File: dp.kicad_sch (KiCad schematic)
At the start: 27 parts, among them J1 DisplayPort_Mini_47272-0001, U1 74AVC4T245_UQFN, U2 FIN1019MTC, U3 TPD4E05U06QDQARQ1_ALT, U4 824012823

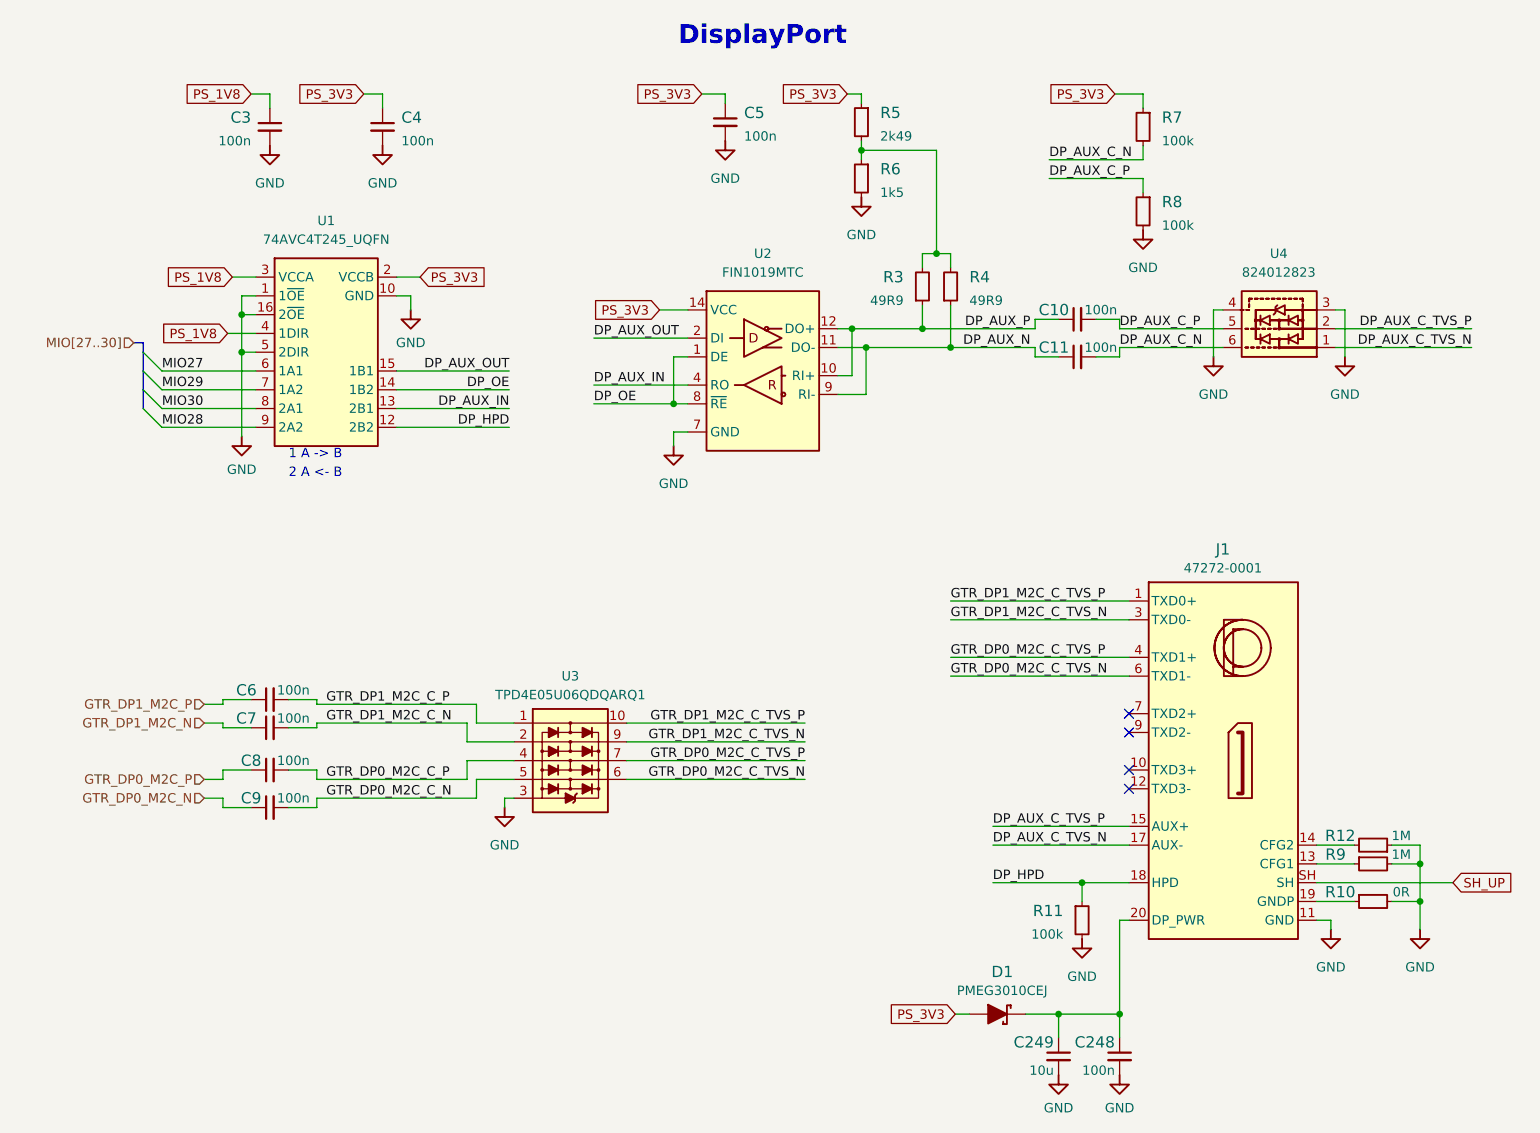
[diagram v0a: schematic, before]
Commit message: [#47975] Add missing ESD diode pass for USB 3.0 and DP interfaces, bump revision
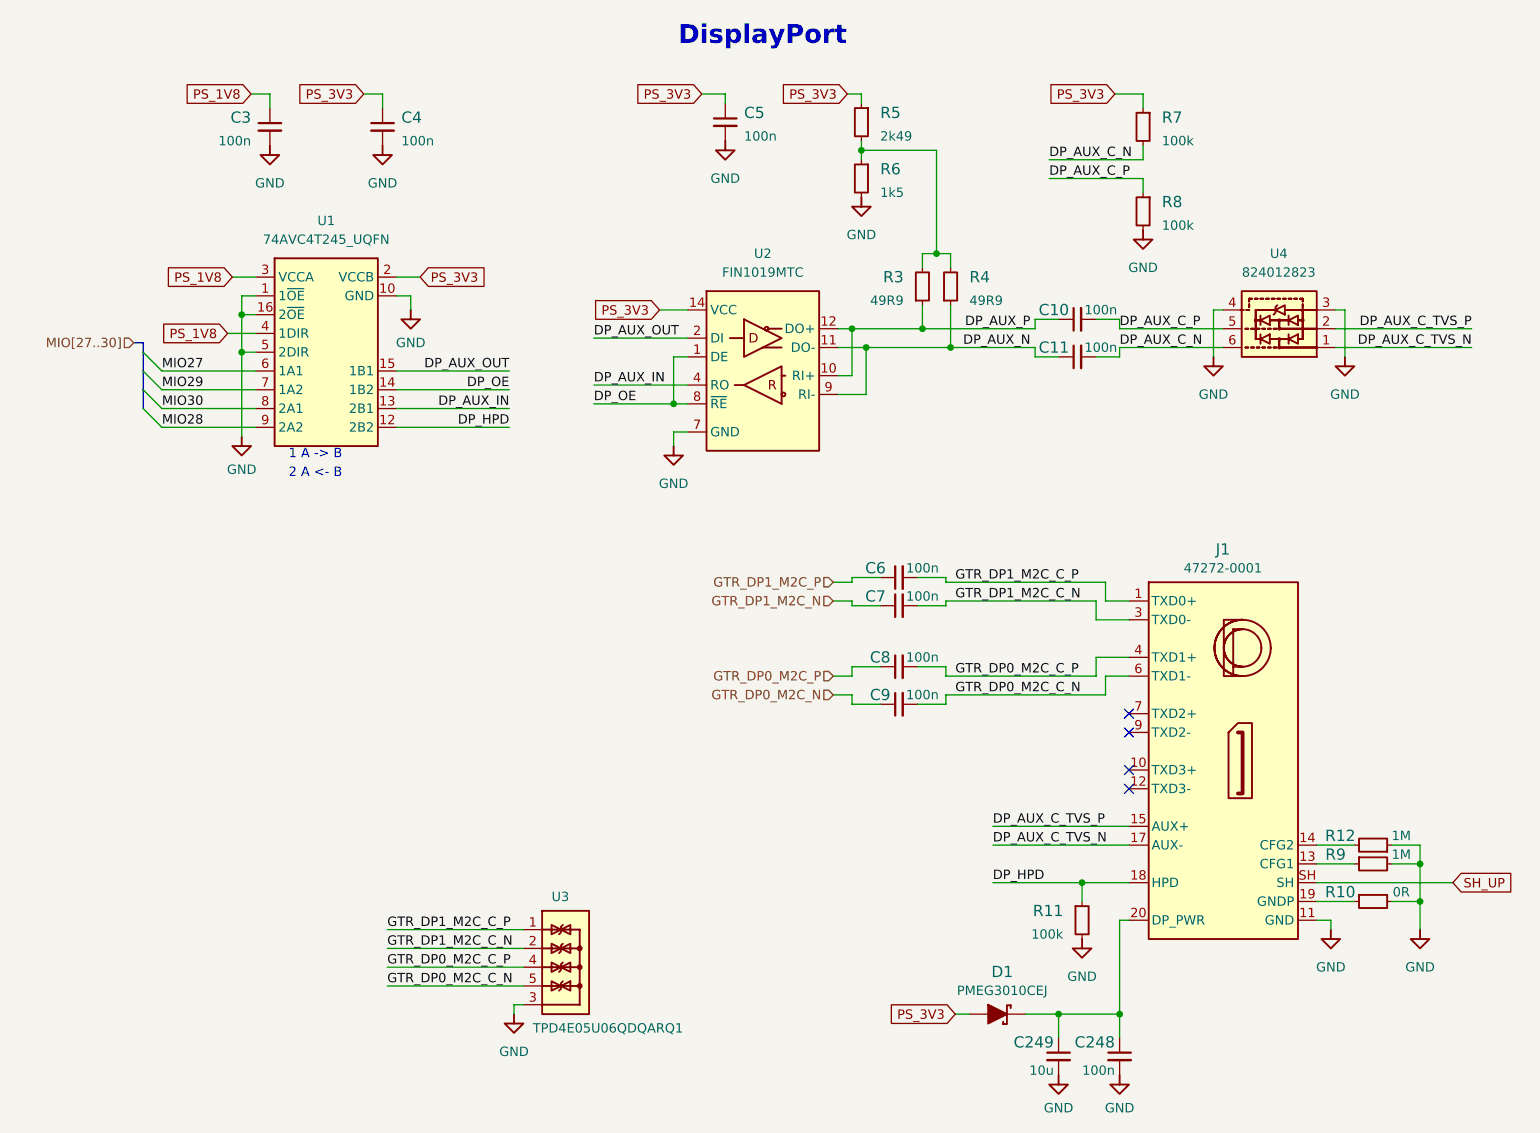
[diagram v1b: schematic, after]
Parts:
- removed U3: TPD4E05U06QDQARQ1_ALT, kria-k26-devboard-footprints:USON-10_2.5x1mm_P0.5mm, symbol kria-k26-devboard:TPD4E05U06QDQARQ1_ALT
- added U3: TPD4E05U06QDQARQ1, antmicro-footprints:USON-10_2.5x1mm_P0.5mm, symbol antmicroTVSDiodes:TPD4E05U06QDQARQ1
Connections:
- net GTR_DP0_M2C_C_TVS_N is gone; now on net GTR_DP0_M2C_C_N: J1.6 (TXD1-)
- net GTR_DP0_M2C_C_TVS_P is gone; now on net GTR_DP0_M2C_C_P: J1.4 (TXD1+)
- net GTR_DP1_M2C_C_TVS_N is gone; now on net GTR_DP1_M2C_C_N: J1.3 (TXD0-)
- net GTR_DP1_M2C_C_TVS_P is gone; now on net GTR_DP1_M2C_C_P: J1.1 (TXD0+)
- net GND: now also U3.3, U3.8
- net GTR_DP0_M2C_C_N: now also U3.5, U3.6
- net GTR_DP0_M2C_C_P: now also U3.4, U3.7
- net GTR_DP1_M2C_C_N: now also U3.2, U3.9
- net GTR_DP1_M2C_C_P: now also U3.1, U3.10
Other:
- moved on the sheet: C6, C7, C8, C9

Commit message: Loclib of the project
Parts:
- U3: footprint antmicro-footprints:USON-10_2.5x1mm_P0.5mm -> kria-k26-devboard-footprints:USON-10_2.5x1mm_P0.5mm; symbol antmicroTVSDiodes:TPD4E05U06QDQARQ1 -> kria-k26-devboard:TPD4E05U06QDQARQ1

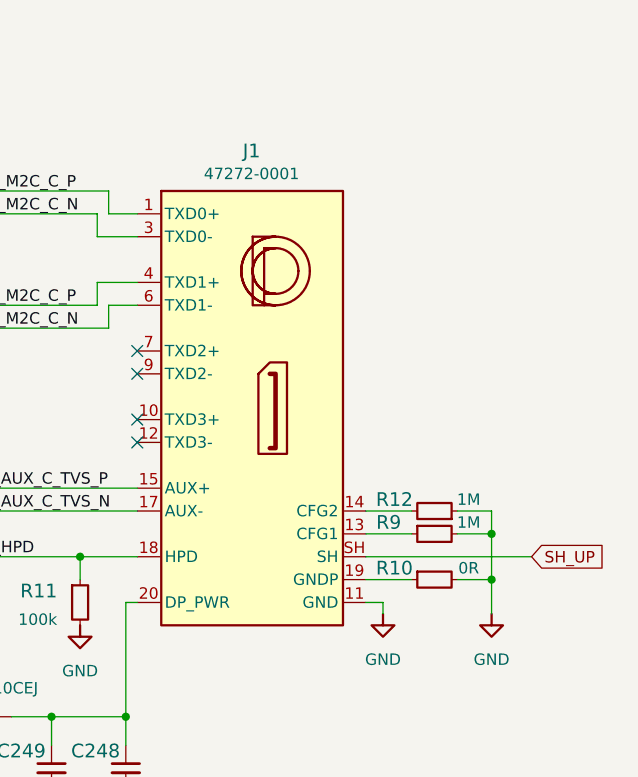
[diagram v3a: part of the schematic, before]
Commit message: [#56935] Update symbol/footprint links; Migrate to KiCad 7
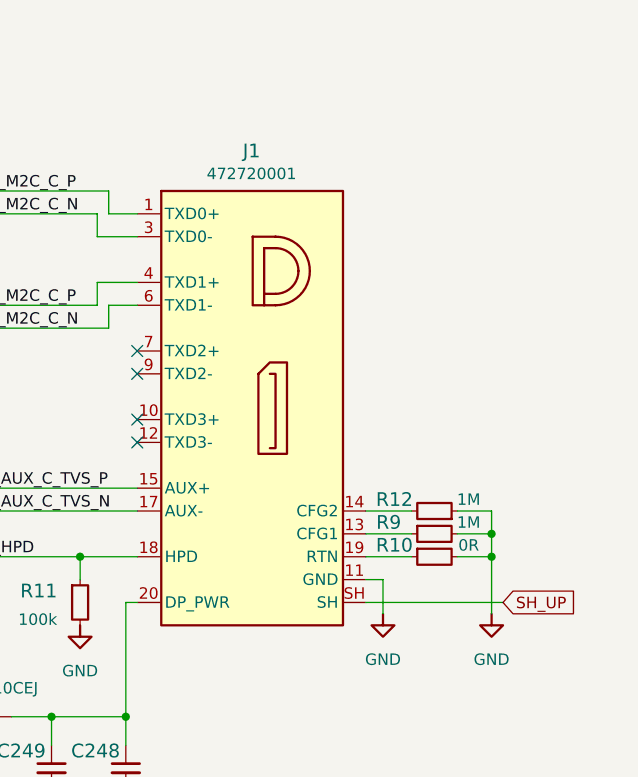
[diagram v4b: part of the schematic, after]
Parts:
- C10, C11, C248, C3, C4, C5, C6, C7, C8, C9: footprint kria-k26-devboard-footprints:C_0402_1005Metric -> antmicro-footprints:C_0402_1005Metric; symbol kria-k26-devboard:C_100n_0402 -> antmicroCapacitors0402:C_100n_0402
- C249: footprint kria-k26-devboard-footprints:C_0402_1005Metric -> antmicro-footprints:C_0402_1005Metric; symbol kria-k26-devboard:C_10u_0402 -> antmicroCapacitors0402:C_10u_0402
- D1: footprint kria-k26-devboard-footprints:D_SOD-323F -> antmicro-footprints:D_SOD-323F; symbol kria-k26-devboard:PMEG3010CE_SOD323 -> antmicroDiodesRectifiersSingle:PMEG3010CE_SOD323
- J1: value DisplayPort_Mini_47272-0001 -> DisplayPort_Molex_472720001; footprint kria-k26-devboard-footprints:DisplayPort_Mini_MOLEX_47272-0001 -> antmicro-footprints:DisplayPort_Receptacle_Molex_472720001; symbol kria-k26-devboard:DisplayPort_Mini_47272-0001 -> antmicroVideoConnectors:DisplayPort_Molex_472720001; MPN 47272-0001 -> 472720001
- R10: footprint kria-k26-devboard-footprints:R_0402_1005Metric -> antmicro-footprints:R_0402_1005Metric; symbol kria-k26-devboard:R_0R_0402 -> antmicroResistors0402:R_0R_0402
- R11, R7, R8: footprint kria-k26-devboard-footprints:R_0402_1005Metric -> antmicro-footprints:R_0402_1005Metric; symbol kria-k26-devboard:R_100k_0402 -> antmicroResistors0402:R_100k_0402
- R12, R9: footprint kria-k26-devboard-footprints:R_0402_1005Metric -> antmicro-footprints:R_0402_1005Metric; symbol kria-k26-devboard:R_1M_0402 -> antmicroResistors0402:R_1M_0402
- R3, R4: footprint kria-k26-devboard-footprints:R_0402_1005Metric -> antmicro-footprints:R_0402_1005Metric; symbol kria-k26-devboard:R_49R9_0402 -> antmicroResistors0402:R_49R9_0402
- R5: footprint kria-k26-devboard-footprints:R_0402_1005Metric -> antmicro-footprints:R_0402_1005Metric; symbol kria-k26-devboard:R_2k49_0402 -> antmicroResistors0402:R_2k49_0402
- R6: footprint kria-k26-devboard-footprints:R_0402_1005Metric -> antmicro-footprints:R_0402_1005Metric; symbol kria-k26-devboard:R_1k5_0402 -> antmicroResistors0402:R_1k5_0402
- U1: footprint kria-k26-devboard-footprints:UQFN-16-1.8x2.6mm_P0.4mm_Texas_RSV0016A -> antmicro-footprints:UQFN-16-1.8x2.6mm_P0.4mm_Texas_RSV0016A; symbol kria-k26-devboard:74AVC4T245_UQFN -> antmicroLogicTranslatorsLevelShifters:74AVC4T245_UQFN
- U2: footprint kria-k26-devboard-footprints:TSSOP-14_4.4x5mm_P0.65mm -> antmicro-footprints:TSSOP-14_4.4x5mm_P0.65mm; symbol kria-k26-devboard:FIN1019MTC -> antmicroInterfaceDriversReceiversTransceivers:FIN1019MTC
- U3: footprint kria-k26-devboard-footprints:USON-10_2.5x1mm_P0.5mm -> antmicro-footprints:USON-10_2.5x1mm_P0.5mm; symbol kria-k26-devboard:TPD4E05U06QDQARQ1 -> antmicroTVSDiodes:TPD4E05U06QDQARQ1
- U4: footprint kria-k26-devboard-footprints:DFN1210-6 -> antmicro-footprints:DFN1210-6; symbol kria-k26-devboard:824012823 -> antmicroTVSDiodes:824012823
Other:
- moved on the sheet: R10

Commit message: [#56935] Loclib
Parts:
- C10, C11, C248, C3, C4, C5, C6, C7, C8, C9: footprint antmicro-footprints:C_0402_1005Metric -> kria-k26-devboard-footprints:C_0402_1005Metric; symbol antmicroCapacitors0402:C_100n_0402 -> kria-k26-devboard:C_100n_0402
- C249: footprint antmicro-footprints:C_0402_1005Metric -> kria-k26-devboard-footprints:C_0402_1005Metric; symbol antmicroCapacitors0402:C_10u_0402 -> kria-k26-devboard:C_10u_0402
- D1: footprint antmicro-footprints:D_SOD-323F -> kria-k26-devboard-footprints:D_SOD-323F; symbol antmicroDiodesRectifiersSingle:PMEG3010CE_SOD323 -> kria-k26-devboard:PMEG3010CE_SOD323
- J1: footprint antmicro-footprints:DisplayPort_Receptacle_Molex_472720001 -> kria-k26-devboard-footprints:DisplayPort_Receptacle_Molex_472720001; symbol antmicroVideoConnectors:DisplayPort_Molex_472720001 -> kria-k26-devboard:DisplayPort_Molex_472720001
- R10: footprint antmicro-footprints:R_0402_1005Metric -> kria-k26-devboard-footprints:R_0402_1005Metric; symbol antmicroResistors0402:R_0R_0402 -> kria-k26-devboard:R_0R_0402
- R11, R7, R8: footprint antmicro-footprints:R_0402_1005Metric -> kria-k26-devboard-footprints:R_0402_1005Metric; symbol antmicroResistors0402:R_100k_0402 -> kria-k26-devboard:R_100k_0402
- R12, R9: footprint antmicro-footprints:R_0402_1005Metric -> kria-k26-devboard-footprints:R_0402_1005Metric; symbol antmicroResistors0402:R_1M_0402 -> kria-k26-devboard:R_1M_0402
- R3, R4: footprint antmicro-footprints:R_0402_1005Metric -> kria-k26-devboard-footprints:R_0402_1005Metric; symbol antmicroResistors0402:R_49R9_0402 -> kria-k26-devboard:R_49R9_0402
- R5: footprint antmicro-footprints:R_0402_1005Metric -> kria-k26-devboard-footprints:R_0402_1005Metric; symbol antmicroResistors0402:R_2k49_0402 -> kria-k26-devboard:R_2k49_0402
- R6: footprint antmicro-footprints:R_0402_1005Metric -> kria-k26-devboard-footprints:R_0402_1005Metric; symbol antmicroResistors0402:R_1k5_0402 -> kria-k26-devboard:R_1k5_0402
- U1: footprint antmicro-footprints:UQFN-16-1.8x2.6mm_P0.4mm_Texas_RSV0016A -> kria-k26-devboard-footprints:UQFN-16-1.8x2.6mm_P0.4mm_Texas_RSV0016A; symbol antmicroLogicTranslatorsLevelShifters:74AVC4T245_UQFN -> kria-k26-devboard:74AVC4T245_UQFN
- U2: footprint antmicro-footprints:TSSOP-14_4.4x5mm_P0.65mm -> kria-k26-devboard-footprints:TSSOP-14_4.4x5mm_P0.65mm; symbol antmicroInterfaceDriversReceiversTransceivers:FIN1019MTC -> kria-k26-devboard:FIN1019MTC
- U3: footprint antmicro-footprints:USON-10_2.5x1mm_P0.5mm -> kria-k26-devboard-footprints:USON-10_2.5x1mm_P0.5mm; symbol antmicroTVSDiodes:TPD4E05U06QDQARQ1 -> kria-k26-devboard:TPD4E05U06QDQARQ1
- U4: footprint antmicro-footprints:DFN1210-6 -> kria-k26-devboard-footprints:DFN1210-6; symbol antmicroTVSDiodes:824012823 -> kria-k26-devboard:824012823
